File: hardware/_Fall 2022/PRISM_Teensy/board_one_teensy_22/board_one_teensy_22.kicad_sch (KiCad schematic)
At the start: 15 parts, among them J1 EAST, J2 CORE_IO, J3 USB_micro, U1 Teensy4.1, U2 BNO055_Breakout, U3 3966

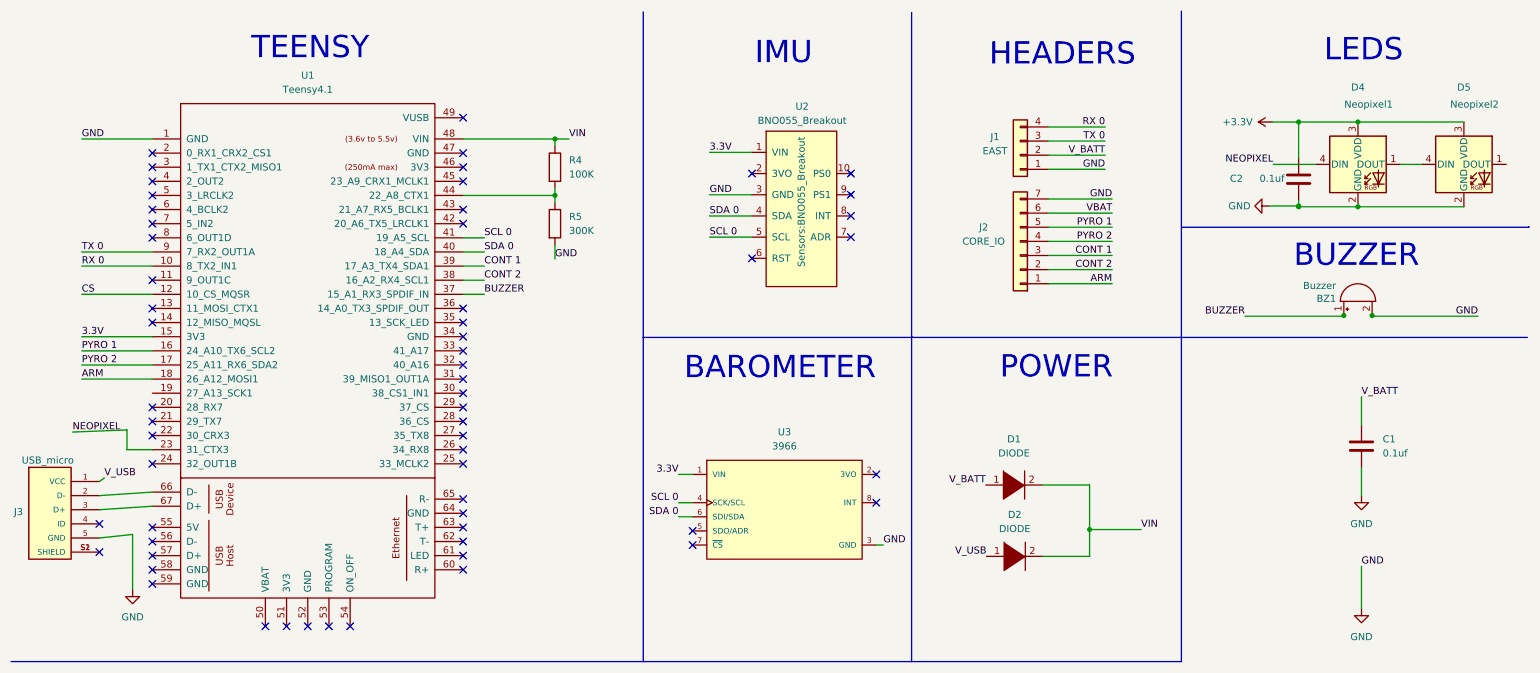
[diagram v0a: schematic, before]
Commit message: Complete PRISM Teensy layout
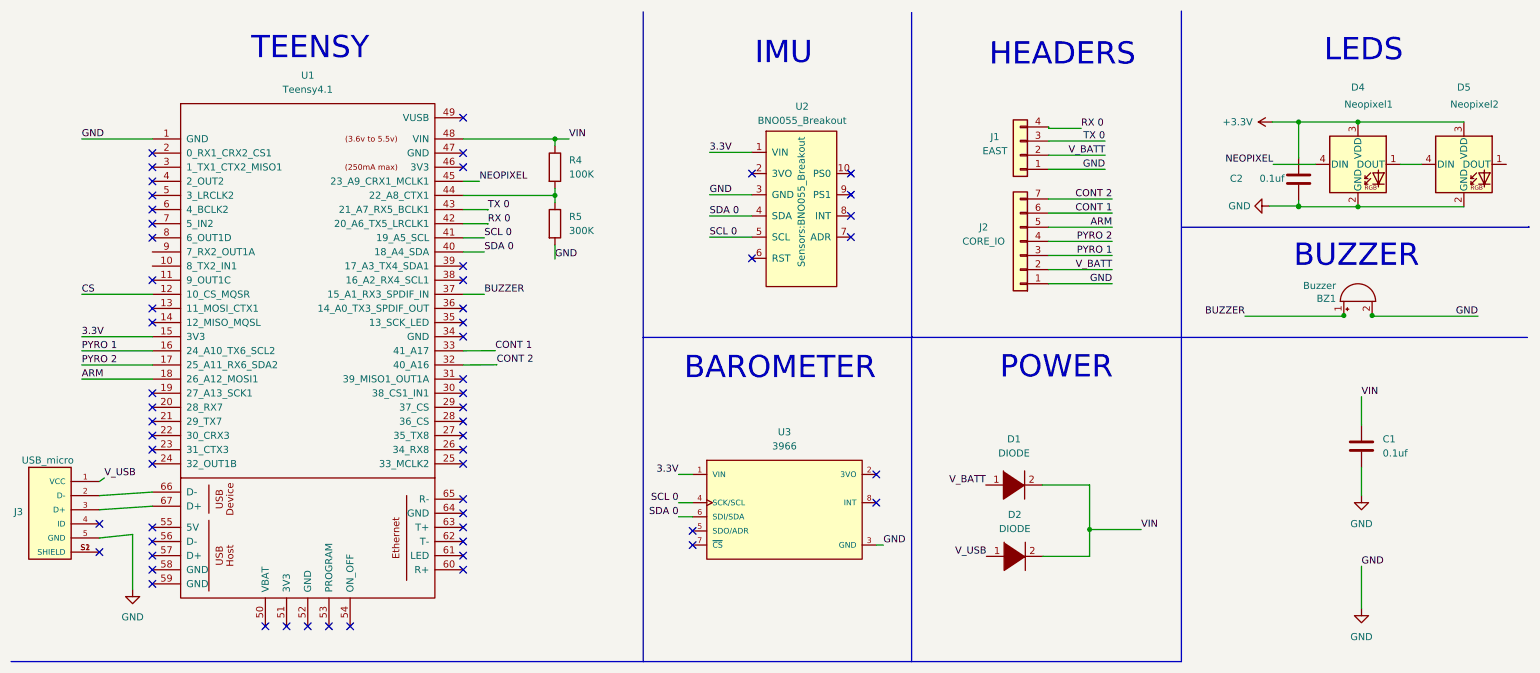
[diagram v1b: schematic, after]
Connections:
- net RX 0  is gone; now on net RX 0: J1.4 (Pin_4)
- net VBAT is gone; now on net CONT 1: J2.6 (Pin_6)
- net ARM: now also J2.5 (Pin_5); no longer J2.1 (Pin_1)
- net CONT 1: now also U1.33 (41_A17); no longer J2.3 (Pin_3), U1.39 (17_A3_TX4_SDA1)
- net CONT 2: now also J2.7 (Pin_7), U1.32 (40_A16); no longer J2.2 (Pin_2), U1.38 (16_A2_RX4_SCL1)
- net GND: now also J2.1 (Pin_1); no longer J2.7 (Pin_7)
- net NEOPIXEL: now also U1.45 (23_A9_CRX1_MCLK1); no longer U1.23 (31_CTX3)
- net PYRO 1: now also J2.3 (Pin_3); no longer J2.5 (Pin_5)
- net RX 0: now also U1.42 (20_A6_TX5_LRCLK1); no longer U1.10 (8_TX2_IN1)
- net TX 0: now also U1.43 (21_A7_RX5_BCLK1); no longer U1.9 (7_RX2_OUT1A)
- net VIN: now also C1.1
- net V_BATT: now also J2.2 (Pin_2); no longer C1.1
- no-connect marks 60 -> 59
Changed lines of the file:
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@@
   (junction (at 243.586 31.877) (diameter 0) (color 0 0 0 0)
   )
+  (no_connect (at 37.465 90.805))
+  (no_connect (at 37.465 80.645))
   (no_connect (at 163.068 44.958))
   (no_connect (at 27.94 104.14))
   (no_connect (at 27.94 109.22))
-  (no_connect (at 93.345 42.545))
   (no_connect (at 93.345 40.005))
   (no_connect (at 93.345 37.465))
@@
   (no_connect (at 37.465 40.005))
   (no_connect (at 37.465 42.545))
-  (no_connect (at 93.345 50.165))
-  (no_connect (at 93.345 47.625))
   (no_connect (at 37.465 60.325))
   (no_connect (at 93.345 70.485))
@@
   (no_connect (at 93.345 80.645))
   (no_connect (at 93.345 78.105))
-  (no_connect (at 93.345 75.565))
-  (no_connect (at 93.345 73.025))
   (no_connect (at 163.068 48.768))
   (no_connect (at 145.288 41.148))
@@
   (no_connect (at 37.465 67.945))
   (no_connect (at 37.465 65.405))
+  (no_connect (at 93.345 57.785))
+  (no_connect (at 93.345 60.325))
   (no_connect (at 163.068 52.578))
   (no_connect (at 145.288 56.388))
@@
     (stroke (width 0) (type default) (color 0 0 0 0))
   )
-  (wire (pts (xy 24.765 55.245) (xy 37.465 55.245))
-    (stroke (width 0) (type default) (color 0 0 0 0))
-  )
   (wire (pts (xy 251.714 66.675) (xy 251.714 66.802))
     (stroke (width 0) (type default) (color 0 0 0 0))
   )
-  (wire (pts (xy 23.114 87.63) (xy 32.893 87.249))
+  (wire (pts (xy 198.628 33.02) (xy 198.628 32.766))
     (stroke (width 0) (type default) (color 0 0 0 0))
   )
@@
     (stroke (width 0) (type default) (color 0 0 0 0))
   )
+  (wire (pts (xy 93.345 50.165) (xy 97.7931 50.165))
+    (stroke (width 0) (type default) (color 0 0 0 0))
+  )
   (wire (pts (xy 132.08 100.33) (xy 134.62 100.33))
     (stroke (width 0) (type default) (color 0 0 0 0))
@@
     (stroke (width 0) (type default) (color 0 0 0 0))
   )
+  (wire (pts (xy 97.7931 47.625) (xy 97.7931 47.6946))
+    (stroke (width 0) (type default) (color 0 0 0 0))
+  )
   (wire (pts (xy 27.94 101.6) (xy 37.465 100.965))
     (stroke (width 0) (type default) (color 0 0 0 0))
   )
-  (wire (pts (xy 32.893 87.249) (xy 32.893 90.805))
-    (stroke (width 0) (type default) (color 0 0 0 0))
-  )
   (wire (pts (xy 210.058 53.34) (xy 198.628 53.34))
     (stroke (width 0) (type default) (color 0 0 0 0))
@@
     (stroke (width 0) (type default) (color 0 0 0 0))
   )
+  (wire (pts (xy 93.345 42.545) (xy 96.2803 42.545))
+    (stroke (width 0) (type default) (color 0 0 0 0))
+  )
   (polyline (pts (xy 173.99 128.905) (xy 173.99 70.358))
     (stroke (width 0) (type default) (color 0 0 0 0))
   )
+  (wire (pts (xy 99.3762 75.5363) (xy 99.3762 75.4893))
+    (stroke (width 0) (type default) (color 0 0 0 0))
+  )
   (wire (pts (xy 261.874 39.497) (xy 265.684 39.497))
     (stroke (width 0) (type default) (color 0 0 0 0))
@@
     (stroke (width 0) (type default) (color 0 0 0 0))
   )
+  (wire (pts (xy 93.345 47.625) (xy 97.7931 47.625))
+    (stroke (width 0) (type default) (color 0 0 0 0))
+  )
   (polyline (pts (xy 222.504 11.938) (xy 222.504 70.612))
     (stroke (width 0) (type default) (color 0 0 0 0))
@@
     (stroke (width 0) (type default) (color 0 0 0 0))
   )
+  (wire (pts (xy 93.345 73.025) (xy 99.1265 72.9963))
+    (stroke (width 0) (type default) (color 0 0 0 0))
+  )
   (polyline (pts (xy 125.73 70.612) (xy 173.99 70.612))
     (stroke (width 0) (type default) (color 0 0 0 0))
@@
     (stroke (width 0) (type default) (color 0 0 0 0))
   )
-  (wire (pts (xy 93.345 57.785) (xy 97.155 57.785))
-    (stroke (width 0) (type default) (color 0 0 0 0))
-  )
   (wire (pts (xy 132.08 102.87) (xy 134.62 102.87))
     (stroke (width 0) (type default) (color 0 0 0 0))
@@
     (stroke (width 0) (type default) (color 0 0 0 0))
   )
-  (wire (pts (xy 93.345 60.325) (xy 97.155 60.325))
+  (wire (pts (xy 97.7931 50.165) (xy 97.7931 50.2346))
     (stroke (width 0) (type default) (color 0 0 0 0))
   )
@@
     (stroke (width 0) (type default) (color 0 0 0 0))
   )
+  (wire (pts (xy 93.345 75.565) (xy 99.3762 75.5363))
+    (stroke (width 0) (type default) (color 0 0 0 0))
+  )
   (wire (pts (xy 109.855 53.975) (xy 109.855 56.515))
     (stroke (width 0) (type default) (color 0 0 0 0))
   )
-  (wire (pts (xy 24.765 57.785) (xy 37.465 57.785))
-    (stroke (width 0) (type default) (color 0 0 0 0))
-  )
   (wire (pts (xy 210.058 60.96) (xy 198.628 60.96))
     (stroke (width 0) (type default) (color 0 0 0 0))
@@
     (stroke (width 0) (type default) (color 0 0 0 0))
   )
-  (wire (pts (xy 32.893 90.805) (xy 37.465 90.805))
-    (stroke (width 0) (type default) (color 0 0 0 0))
-  )
   (polyline (pts (xy 222.504 128.905) (xy 222.504 70.612))
     (stroke (width 0) (type default) (color 0 0 0 0))
@@
     (stroke (width 0) (type default) (color 0 0 0 0))
   )
+  (wire (pts (xy 204.47 33.02) (xy 198.628 33.02))
+    (stroke (width 0) (type default) (color 0 0 0 0))
+  )
   (wire (pts (xy 109.855 34.925) (xy 112.395 34.925))
     (stroke (width 0) (type default) (color 0 0 0 0))
@@
     (stroke (width 0) (type default) (color 0 0 0 0))
   )
-  (wire (pts (xy 208.788 32.766) (xy 198.628 32.766))
-    (stroke (width 0) (type default) (color 0 0 0 0))
-  )
   (wire (pts (xy 24.765 78.105) (xy 37.465 78.105))
     (stroke (width 0) (type default) (color 0 0 0 0))
@@
     (effects (font (size 1.27 1.27)) (justify left bottom))
   )
-  (label "RX 0" (at 24.765 57.785 0)
-    (effects (font (size 1.27 1.27)) (justify left bottom))
-  )
   (label "TX 0" (at 208.788 35.306 180)
     (effects (font (size 1.27 1.27)) (justify right bottom))
@@
     (effects (font (size 1.27 1.27)) (justify left bottom))
   )
-  (label "ARM" (at 210.058 60.96 180)
+  (label "GND" (at 210.058 60.96 180)
     (effects (font (size 1.27 1.27)) (justify right bottom))
   )
@@
     (effects (font (size 1.27 1.27)) (justify right bottom))
   )
-  (label "CONT 2" (at 97.155 60.325 0)
-    (effects (font (size 1.27 1.27)) (justify left bottom))
-  )
   (label "PYRO 2" (at 210.058 53.34 180)
     (effects (font (size 1.27 1.27)) (justify right bottom))
@@
     (effects (font (size 1.27 1.27)) (justify left bottom))
   )
-  (label "CONT 2" (at 210.058 58.42 180)
-    (effects (font (size 1.27 1.27)) (justify right bottom))
+  (label "V_BATT" (at 210.058 58.42 180)
+    (effects (font (size 1.27 1.27)) (justify right bottom))
+  )
+  (label "CONT 1" (at 99.1265 72.9963 0)
+    (effects (font (size 1.27 1.27)) (justify left bottom))
   )
   (label "V_USB" (at 187.452 109.982 180)
@@
     (effects (font (size 1.27 1.27)) (justify right bottom))
   )
-  (label "CONT 1" (at 97.155 57.785 0)
-    (effects (font (size 1.27 1.27)) (justify left bottom))
-  )
   (label "GND" (at 137.668 44.958 0)
     (effects (font (size 1.27 1.27)) (justify left bottom))
   )
+  (label "RX 0" (at 204.47 33.02 0)
+    (effects (font (size 1.27 1.27)) (justify left bottom))
+  )
   (label "GND" (at 254.889 111.76 0)
     (effects (font (size 1.27 1.27)) (justify left bottom))
@@
     (effects (font (size 1.27 1.27)) (justify right bottom))
   )
-  (label "GND" (at 210.058 45.72 180)
+  (label "RX 0" (at 97.7931 50.2346 0)
+    (effects (font (size 1.27 1.27)) (justify left bottom))
+  )
+  (label "CONT 2" (at 210.058 45.72 180)
     (effects (font (size 1.27 1.27)) (justify right bottom))
   )
@@
     (effects (font (size 1.27 1.27)) (justify left bottom))
   )
-  (label "TX 0" (at 24.765 55.245 0)
-    (effects (font (size 1.27 1.27)) (justify left bottom))
-  )
   (label "SDA 0" (at 97.155 55.245 0)
     (effects (font (size 1.27 1.27)) (justify left bottom))
@@
     (effects (font (size 1.27 1.27)) (justify left bottom))
   )
-  (label "RX 0 " (at 208.788 32.766 180)
-    (effects (font (size 1.27 1.27)) (justify right bottom))
-  )
-  (label "V_BATT" (at 254.889 81.28 0)
-    (effects (font (size 1.27 1.27)) (justify left bottom))
-  )
-  (label "VBAT" (at 210.058 48.26 180)
-    (effects (font (size 1.27 1.27)) (justify right bottom))
+  (label "VIN" (at 254.889 81.28 0)
+    (effects (font (size 1.27 1.27)) (justify left bottom))
+  )
+  (label "TX 0" (at 97.7931 47.6946 0)
+    (effects (font (size 1.27 1.27)) (justify left bottom))
+  )
+  (label "CONT 1" (at 210.058 48.26 180)
+    (effects (font (size 1.27 1.27)) (justify right bottom))
+  )
+  (label "CONT 2" (at 99.3762 75.4893 0)
+    (effects (font (size 1.27 1.27)) (justify left bottom))
   )
   (label "GND" (at 275.844 66.802 180)
@@
     (effects (font (size 1.27 1.27)) (justify left bottom))
   )
+  (label "NEOPIXEL" (at 96.2803 42.545 0)
+    (effects (font (size 1.27 1.27)) (justify left bottom))
+  )
   (label "V_BATT" (at 187.325 97.155 180)
     (effects (font (size 1.27 1.27)) (justify right bottom))
   )
-  (label "NEOPIXEL" (at 23.114 87.63 0)
-    (effects (font (size 1.27 1.27)) (justify left bottom))
-  )
   (label "GND" (at 24.765 34.925 0)
     (effects (font (size 1.27 1.27)) (justify left bottom))
@@
     (effects (font (size 1.27 1.27)) (justify left bottom))
   )
-  (label "PYRO 1" (at 210.058 50.8 180)
+  (label "ARM" (at 210.058 50.8 180)
     (effects (font (size 1.27 1.27)) (justify right bottom))
   )
@@
     (effects (font (size 1.27 1.27)) (justify left bottom))
   )
-  (label "CONT 1" (at 210.058 55.88 180)
-    (effects (font (size 1.27 1.27)) (justify right bottom))
-  )
+  (label "PYRO 1" (at 210.058 55.88 180)
+    (effects (font (size 1.27 1.27)) (justify right bottom))
+  )
